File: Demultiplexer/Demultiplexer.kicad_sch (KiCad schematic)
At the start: 1 part, among them J101 USB_A

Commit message: Working on input stage
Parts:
- J101: footprint (none) -> Connector_USB:USB_A_Molex_67643_Horizontal
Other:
- sheet Input Selectors ports: added a_{0}, a_{1}; removed none

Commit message: Working on decoder stage
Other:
- added sheet Decoder (Decoder.kicad_sch)
- added sheet NOT Gates (NOTGates.kicad_sch)

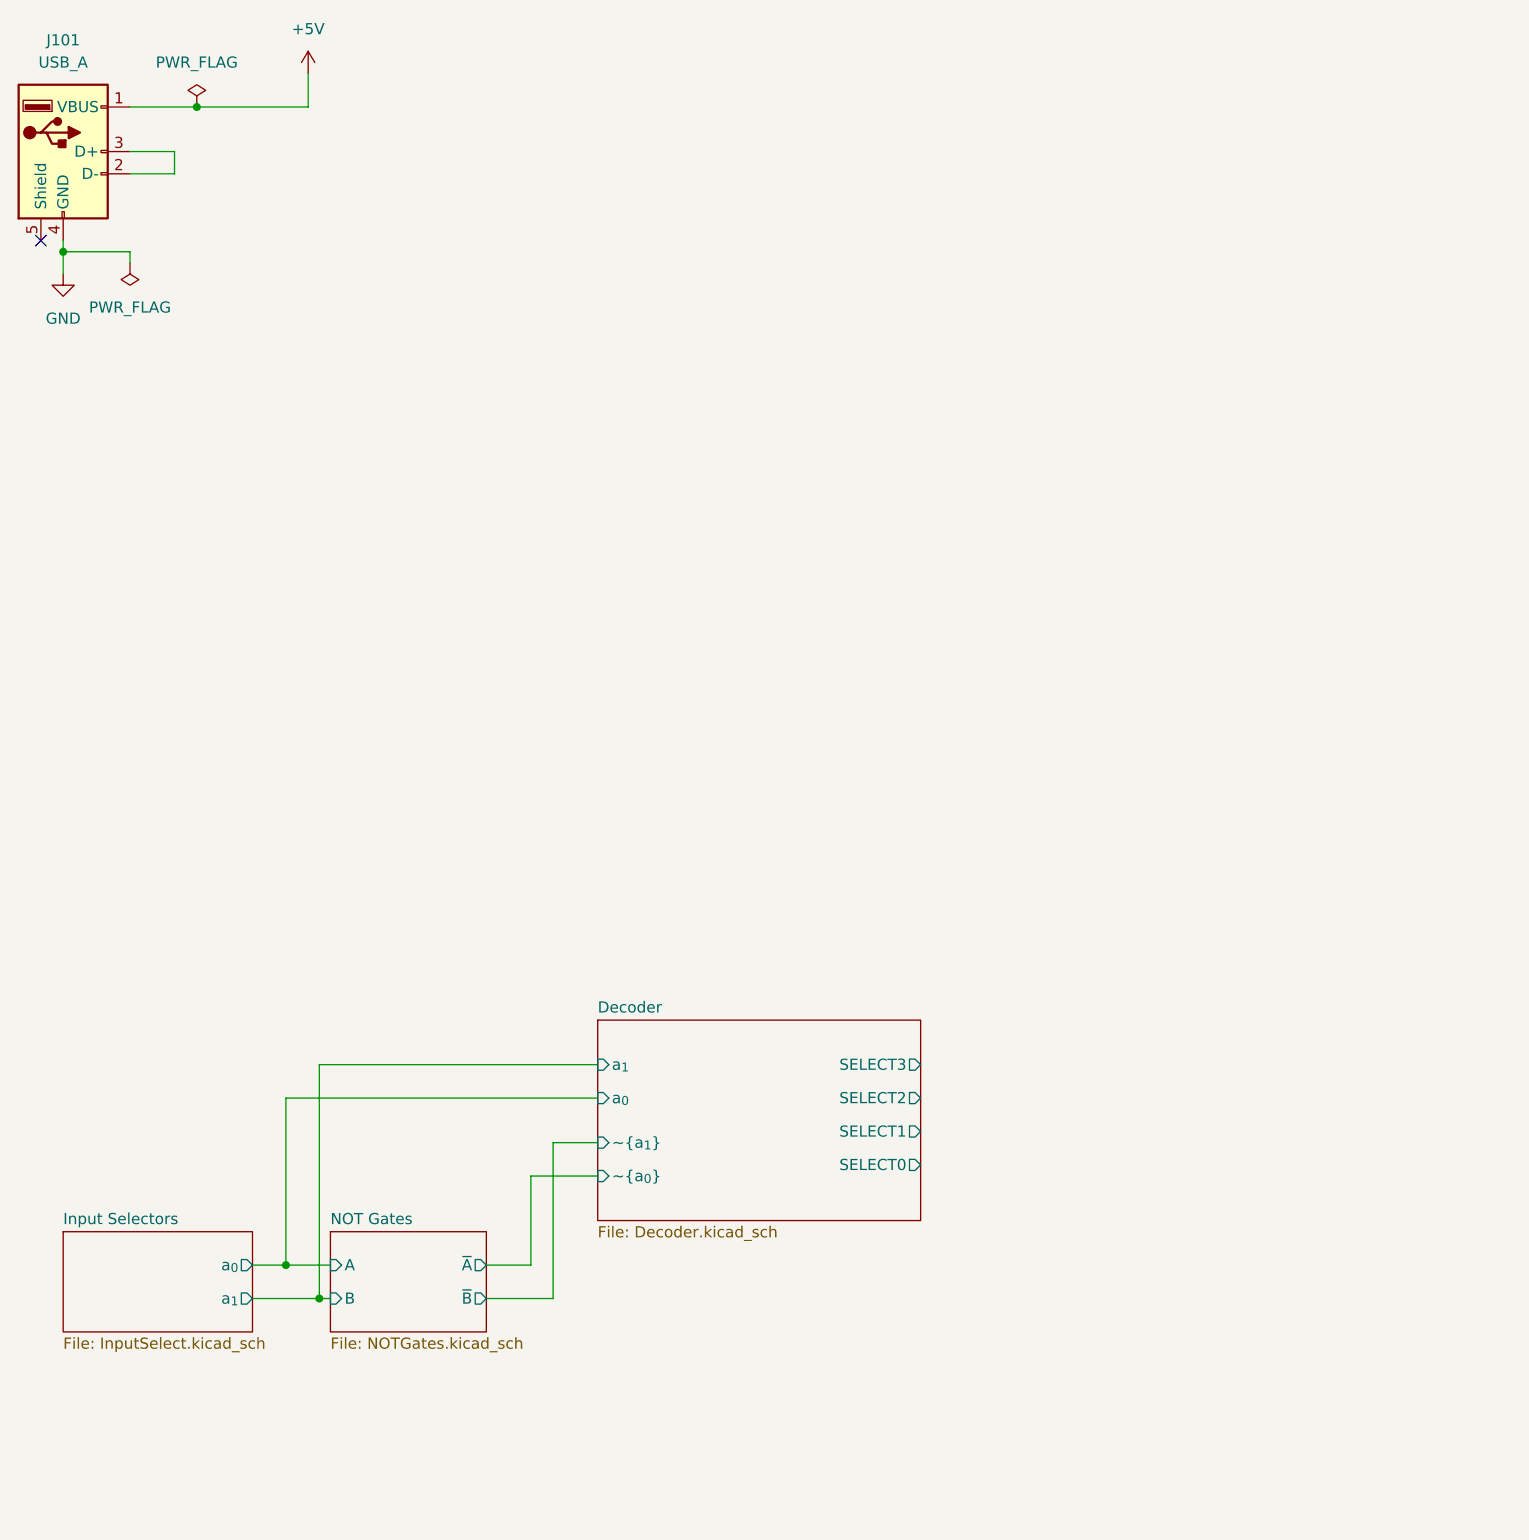
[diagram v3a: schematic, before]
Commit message: Rethinking NOT gates and starting on output
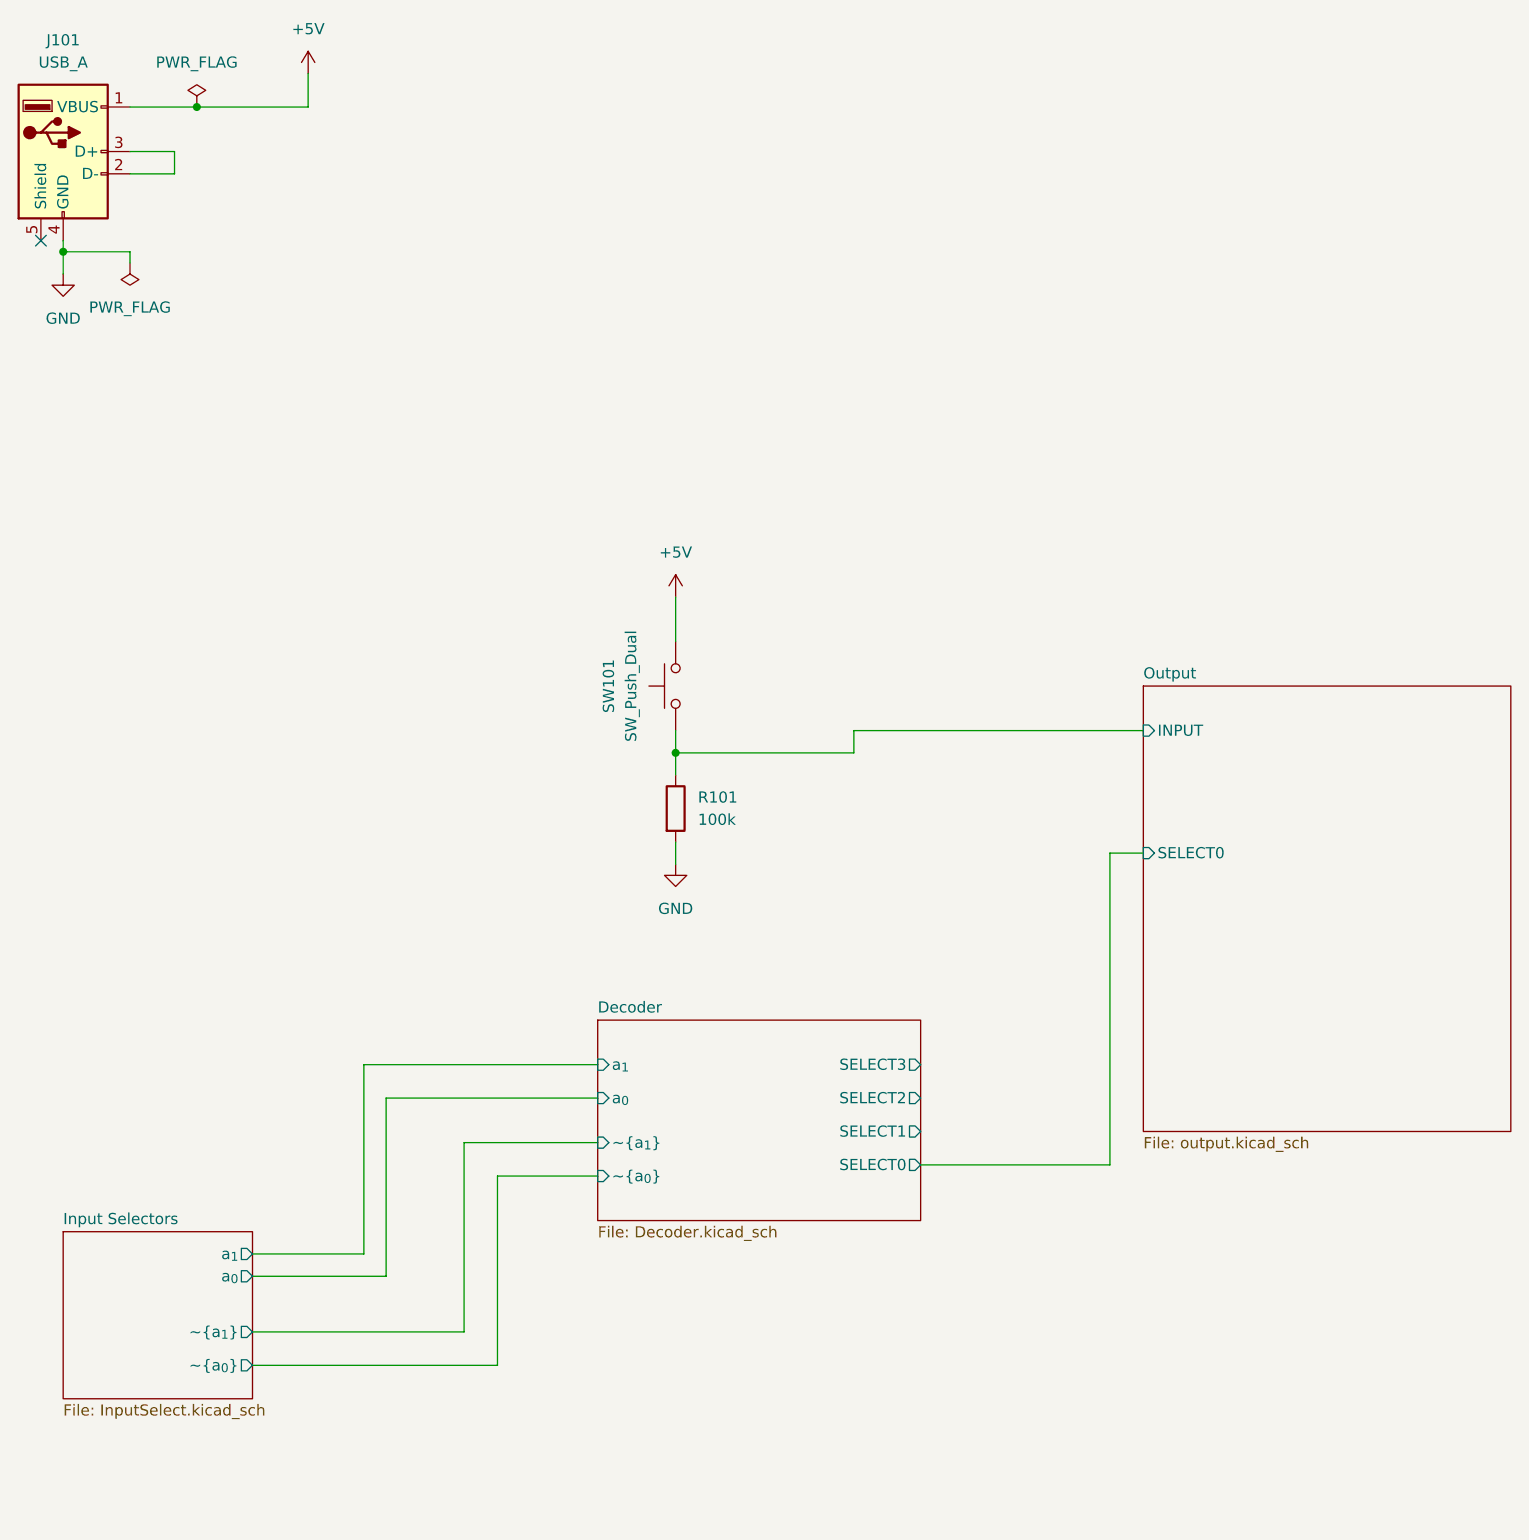
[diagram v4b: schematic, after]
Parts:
- added R101: 100k, Resistor_THT:R_Axial_DIN0207_L6.3mm_D2.5mm_P7.62mm_Horizontal, symbol Device:R
- added SW101: SW_Push_Dual, Button_Switch_THT:SW_PUSH_6mm_H4.3mm, symbol Switch:SW_Push
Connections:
- net +5V: now also SW101.2
- net GND: now also R101.2
- new net Output/INPUT: R101.1, SW101.1
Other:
- removed sheet NOT Gates
- added sheet Output (output.kicad_sch)
- sheet Input Selectors ports: added ~{a_{0}}, ~{a_{1}}; removed none

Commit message: Finish roughing out board
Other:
- sheet Output ports: added SELECT1; removed none
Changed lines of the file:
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@@
+    (stroke (width 0) (type default) (color 0 0 0 0))
+  )
+  (wire (pts (xy 127 143.51) (xy 147.32 143.51))
     (stroke (width 0) (type default) (color 0 0 0 0))
   )
@@
     (stroke (width 0) (type default) (color 0 0 0 0))
   )
+  (wire (pts (xy 147.32 109.22) (xy 152.4 109.22))
+    (stroke (width 0) (type default) (color 0 0 0 0))
+  )
   (wire (pts (xy 66.04 139.7) (xy 90.17 139.7))
     (stroke (width 0) (type default) (color 0 0 0 0))
@@
   )
   (wire (pts (xy 63.5 157.48) (xy 63.5 135.89))
+    (stroke (width 0) (type default) (color 0 0 0 0))
+  )
+  (wire (pts (xy 147.32 143.51) (xy 147.32 109.22))
     (stroke (width 0) (type default) (color 0 0 0 0))
   )
@@
       (effects (font (size 1.27 1.27)) (justify left))
     )
+    (pin "SELECT1" input (at 152.4 109.22 180)
+      (effects (font (size 1.27 1.27)) (justify left))
+    )
   )
   (sheet_instances
@@
       (reference "#PWR0404") (unit 1) (value "GND") (footprint "")
     )
+    (path "/873eee0e-8c95-42b4-854b-83e5f26d3cf0/3d6b605a-f276-472b-9d47-e48ea630afd7"
+      (reference "#PWR0405") (unit 1) (value "+5V") (footprint "")
+    )
+    (path "/873eee0e-8c95-42b4-854b-83e5f26d3cf0/7cd9d5e7-72a4-4258-856c-2c9252e68680"
+      (reference "#PWR0406") (unit 1) (value "GND") (footprint "")
+    )
     (path "/873eee0e-8c95-42b4-854b-83e5f26d3cf0/98001a62-7029-4ff5-b750-25bd2055ad82"
-      (reference "#PWR0405") (unit 1) (value "GND") (footprint "")
+      (reference "#PWR0407") (unit 1) (value "GND") (footprint "")
     )
     (path "/873eee0e-8c95-42b4-854b-83e5f26d3cf0/64ccf30d-e755-431e-8e0e-a35e5f300061"
-      (reference "#PWR0406") (unit 1) (value "GND") (footprint "")
+      (reference "#PWR0408") (unit 1) (value "GND") (footprint "")
+    )
+    (path "/873eee0e-8c95-42b4-854b-83e5f26d3cf0/38d8f9b0-7ab0-4b07-81d0-2ab78f89f6a0"
+      (reference "#PWR0409") (unit 1) (value "GND") (footprint "")
+    )
+    (path "/873eee0e-8c95-42b4-854b-83e5f26d3cf0/eca7ab37-1f3d-442c-b5fd-49dc053a4976"
+      (reference "#PWR0410") (unit 1) (value "GND") (footprint "")
+    )
+    (path "/873eee0e-8c95-42b4-854b-83e5f26d3cf0/5e0d414a-3bc5-4def-b9d4-1627caa03854"
+      (reference "#PWR0411") (unit 1) (value "+5V") (footprint "")
+    )
+    (path "/873eee0e-8c95-42b4-854b-83e5f26d3cf0/ebfadff7-cd16-4361-8e10-82d9d5993f2c"
+      (reference "#PWR0412") (unit 1) (value "GND") (footprint "")
     )
     (path "/873eee0e-8c95-42b4-854b-83e5f26d3cf0/9e04d472-e47e-425f-8cbc-81fb21698df3"
-      (reference "#PWR0407") (unit 1) (value "GND") (footprint "")
+      (reference "#PWR0413") (unit 1) (value "GND") (footprint "")
     )
     (path "/873eee0e-8c95-42b4-854b-83e5f26d3cf0/1c23e072-5384-4ea5-abd5-02a7d0caeac3"
-      (reference "#PWR0408") (unit 1) (value "GND") (footprint "")
+      (reference "#PWR0414") (unit 1) (value "GND") (footprint "")
+    )
+    (path "/873eee0e-8c95-42b4-854b-83e5f26d3cf0/59b45acb-aaa0-4f28-ad97-75f4cbe0ce70"
+      (reference "#PWR0415") (unit 1) (value "GND") (footprint "")
+    )
+    (path "/873eee0e-8c95-42b4-854b-83e5f26d3cf0/1a26db46-a97d-45b9-9411-f1baae12007d"
+      (reference "#PWR0416") (unit 1) (value "GND") (footprint "")
     )
     (path "/1dd65dd8-2e56-4931-888b-7cbfb86751c0/7fbff46a-4185-4263-9d94-9ea8df782ad9"
@@
       (reference "C402") (unit 1) (value "100nF") (footprint "Capacitor_THT:C_Disc_D5.0mm_W2.5mm_P5.00mm")
     )
+    (path "/873eee0e-8c95-42b4-854b-83e5f26d3cf0/78aabde5-8409-4368-91a4-11b2704bde15"
+      (reference "C403") (unit 1) (value "100nF") (footprint "Capacitor_THT:C_Disc_D5.0mm_W2.5mm_P5.00mm")
+    )
+    (path "/873eee0e-8c95-42b4-854b-83e5f26d3cf0/b8957f21-e1aa-481a-bafc-770410cb4b18"
+      (reference "C404") (unit 1) (value "100nF") (footprint "Capacitor_THT:C_Disc_D5.0mm_W2.5mm_P5.00mm")
+    )
     (path "/1dd65dd8-2e56-4931-888b-7cbfb86751c0/637b50ff-7fbc-47ea-b727-41b31c0c4cf5"
       (reference "D201") (unit 1) (value "LED") (footprint "LED_THT:LED_D5.0mm")
@@
       (reference "D402") (unit 1) (value "LED") (footprint "LED_THT:LED_D5.0mm")
     )
+    (path "/873eee0e-8c95-42b4-854b-83e5f26d3cf0/435e0a78-9936-404f-992b-4a3c8c38525f"
+      (reference "D403") (unit 1) (value "LED") (footprint "LED_THT:LED_D5.0mm")
+    )
+    (path "/873eee0e-8c95-42b4-854b-83e5f26d3cf0/eeeee393-a768-43bc-8f4b-cf5a250951f1"
+      (reference "D404") (unit 1) (value "LED") (footprint "LED_THT:LED_D5.0mm")
+    )
     (path "/1b3b5b65-1ebd-4e15-b32a-216a4a57c257"
       (reference "J101") (unit 1) (value "USB_A") (footprint "Connector_USB:USB_A_Molex_67643_Horizontal")
@@
       (reference "R402") (unit 1) (value "4k7") (footprint "Resistor_THT:R_Axial_DIN0207_L6.3mm_D2.5mm_P7.62mm_Horizontal")
     )
+    (path "/873eee0e-8c95-42b4-854b-83e5f26d3cf0/e3fe1e0a-773e-402f-8ecd-6589e808b489"
+      (reference "R403") (unit 1) (value "4k7") (footprint "Resistor_THT:R_Axial_DIN0207_L6.3mm_D2.5mm_P7.62mm_Horizontal")
+    )
+    (path "/873eee0e-8c95-42b4-854b-83e5f26d3cf0/80dcf60d-e018-4d5b-9878-8f4dcfe64f2d"
+      (reference "R404") (unit 1) (value "4k7") (footprint "Resistor_THT:R_Axial_DIN0207_L6.3mm_D2.5mm_P7.62mm_Horizontal")
+    )
     (path "/d095e445-2219-4fd1-bbb7-0562e3eb0c6c"
       (reference "SW101") (unit 1) (value "SW_Push_Dual") (footprint "Button_Switch_THT:SW_PUSH_6mm_H4.3mm")
@@
       (reference "U402") (unit 5) (value "74HC00") (footprint "Package_DIP:DIP-14_W7.62mm_Socket")
     )
-  )
+    (path "/873eee0e-8c95-42b4-854b-83e5f26d3cf0/1682f1fa-59dd-44ad-a2db-8e4f004e1e98"
+      (reference "U403") (unit 1) (value "74HC00") (footprint "")
+    )
+    (path "/873eee0e-8c95-42b4-854b-83e5f26d3cf0/9c2b03da-92ba-4557-b312-f915581db0ae"
+      (reference "U403") (unit 2) (value "74HC00") (footprint "")
+    )
+    (path "/873eee0e-8c95-42b4-854b-83e5f26d3cf0/69a15808-9c1c-474e-8376-cbd04b167f49"
+      (reference "U403") (unit 3) (value "74HC00") (footprint "")
+    )
+    (path "/873eee0e-8c95-42b4-854b-83e5f26d3cf0/3ef87068-695f-43ab-8035-ffe9fb0e350f"
+      (reference "U403") (unit 4) (value "74HC00") (footprint "")
+    )
+    (path "/873eee0e-8c95-42b4-854b-83e5f26d3cf0/faf748a0-0904-41f7-ac57-99ff2c717ec3"
+      (reference "U403") (unit 5) (value "74HC00") (footprint "Package_DIP:DIP-14_W7.62mm_Socket")
+    )
+    (path "/873eee0e-8c95-42b4-854b-83e5f26d3cf0/9c29945f-778d-438f-8cf0-722062b8890a"
+      (reference "U404") (unit 1) (value "74HC00") (footprint "")
+    )
+    (path "/873eee0e-8c95-42b4-854b-83e5f26d3cf0/e4bf9b96-bf16-4162-8cf6-9e38826f3196"
+      (reference "U404") (unit 2) (value "74HC00") (footprint "")
+    )
+    (path "/873eee0e-8c95-42b4-854b-83e5f26d3cf0/b4fc72fb-f8b0-4cbe-9384-e19a1e1fa461"
+      (reference "U404") (unit 3) (value "74HC00") (footprint "")
+    )
+    (path "/873eee0e-8c95-42b4-854b-83e5f26d3cf0/98ffe1e4-36f5-4d1a-8ba4-533316da28f5"
+      (reference "U404") (unit 4) (value "74HC00") (footprint "")
+    )
+    (path "/873eee0e-8c95-42b4-854b-83e5f26d3cf0/1198cc47-d7a8-4cde-ae3f-4800f6997559"
+      (reference "U404") (unit 5) (value "74HC00") (footprint "Package_DIP:DIP-14_W7.62mm_Socket")
+    )
+  )

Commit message: Working on routing
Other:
- sheet Output ports: added SELECT2, SELECT3; removed none
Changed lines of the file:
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@@
+    (stroke (width 0) (type default) (color 0 0 0 0))
+  )
+  (wire (pts (xy 144.78 104.14) (xy 152.4 104.14))
+    (stroke (width 0) (type default) (color 0 0 0 0))
+  )
+  (wire (pts (xy 146.05 106.68) (xy 152.4 106.68))
     (stroke (width 0) (type default) (color 0 0 0 0))
   )
@@
     (stroke (width 0) (type default) (color 0 0 0 0))
   )
+  (wire (pts (xy 146.05 139.7) (xy 146.05 106.68))
+    (stroke (width 0) (type default) (color 0 0 0 0))
+  )
   (wire (pts (xy 148.59 147.32) (xy 148.59 111.76))
     (stroke (width 0) (type default) (color 0 0 0 0))
@@
     (stroke (width 0) (type default) (color 0 0 0 0))
   )
+  (wire (pts (xy 127 135.89) (xy 144.78 135.89))
+    (stroke (width 0) (type default) (color 0 0 0 0))
+  )
   (wire (pts (xy 99.06 110.49) (xy 99.06 113.03))
     (stroke (width 0) (type default) (color 0 0 0 0))
@@
     (stroke (width 0) (type default) (color 0 0 0 0))
   )
+  (wire (pts (xy 144.78 135.89) (xy 144.78 104.14))
+    (stroke (width 0) (type default) (color 0 0 0 0))
+  )
   (wire (pts (xy 29.21 41.91) (xy 29.21 43.18))
     (stroke (width 0) (type default) (color 0 0 0 0))
@@
   )
   (wire (pts (xy 50.8 160.02) (xy 66.04 160.02))
+    (stroke (width 0) (type default) (color 0 0 0 0))
+  )
+  (wire (pts (xy 127 139.7) (xy 146.05 139.7))
     (stroke (width 0) (type default) (color 0 0 0 0))
   )
@@
       (effects (font (size 1.27 1.27)) (justify left))
     )
+    (pin "SELECT2" input (at 152.4 106.68 180)
+      (effects (font (size 1.27 1.27)) (justify left))
+    )
+    (pin "SELECT3" input (at 152.4 104.14 180)
+      (effects (font (size 1.27 1.27)) (justify left))
+    )
